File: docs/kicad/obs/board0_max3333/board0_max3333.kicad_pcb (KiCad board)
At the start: 2 copper layers, 100.3 x 91.4 mm, 38 parts, among them J1 INST_POWER, J10 12V_TEST, J11 5V_TEST, J12 SN65HVD230, J13 CAN_TERMINATOR, J14 MAX3232, J15 GPS_IN, J2 NMEA2000, J3 NMEA2000, J4 83A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

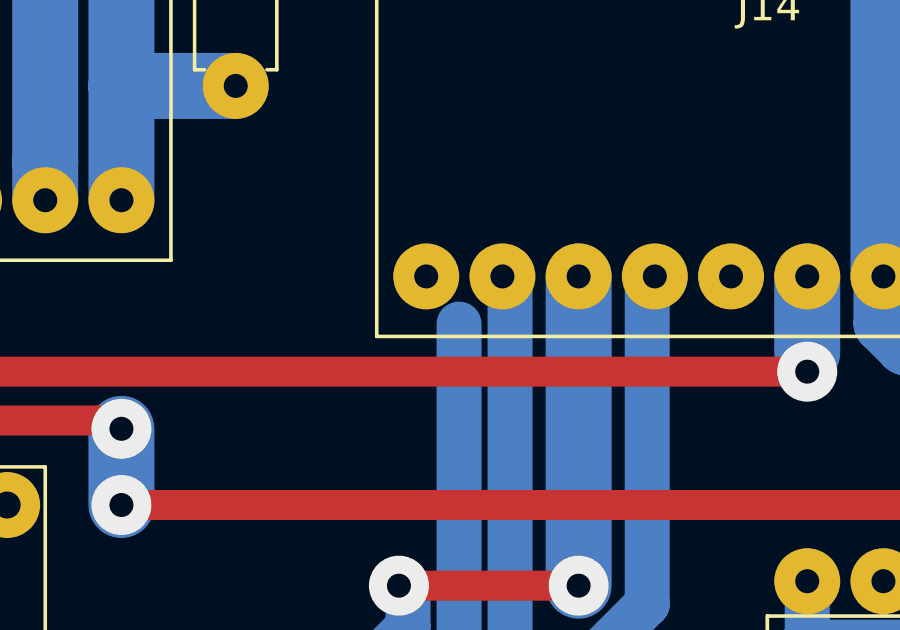
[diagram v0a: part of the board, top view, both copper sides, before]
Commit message: create actual boat teensyBoat pcb board1;  move other kicad stuff to _obs; add/fix kicad footprints
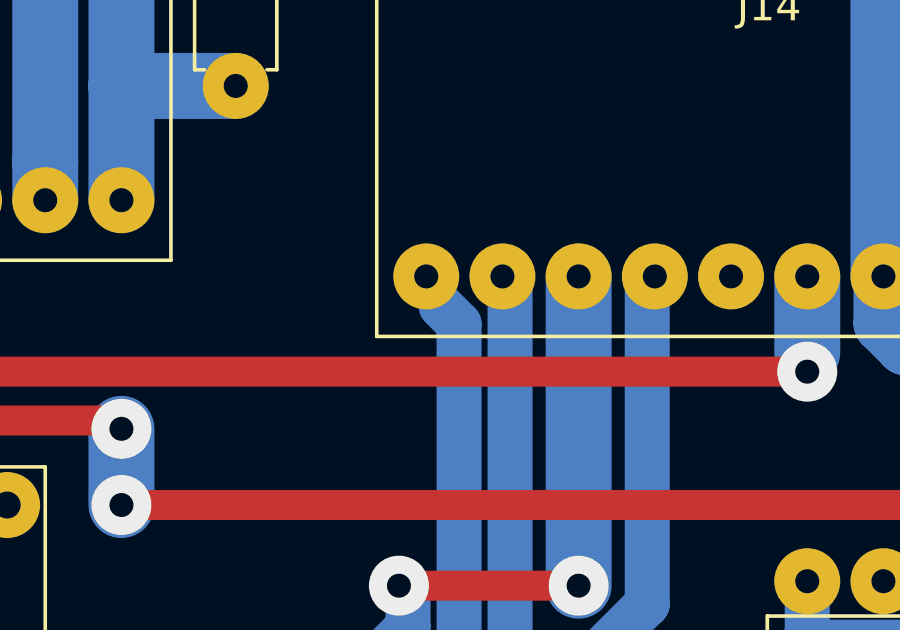
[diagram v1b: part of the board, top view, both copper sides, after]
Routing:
- net RX4: track 32.1 -> 33.0 mm
